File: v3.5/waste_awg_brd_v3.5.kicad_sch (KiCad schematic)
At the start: 24 parts, among them J1 Conn_01x06, U1 74HC595, U2 74HC595, U3 CA56-12CGKWA

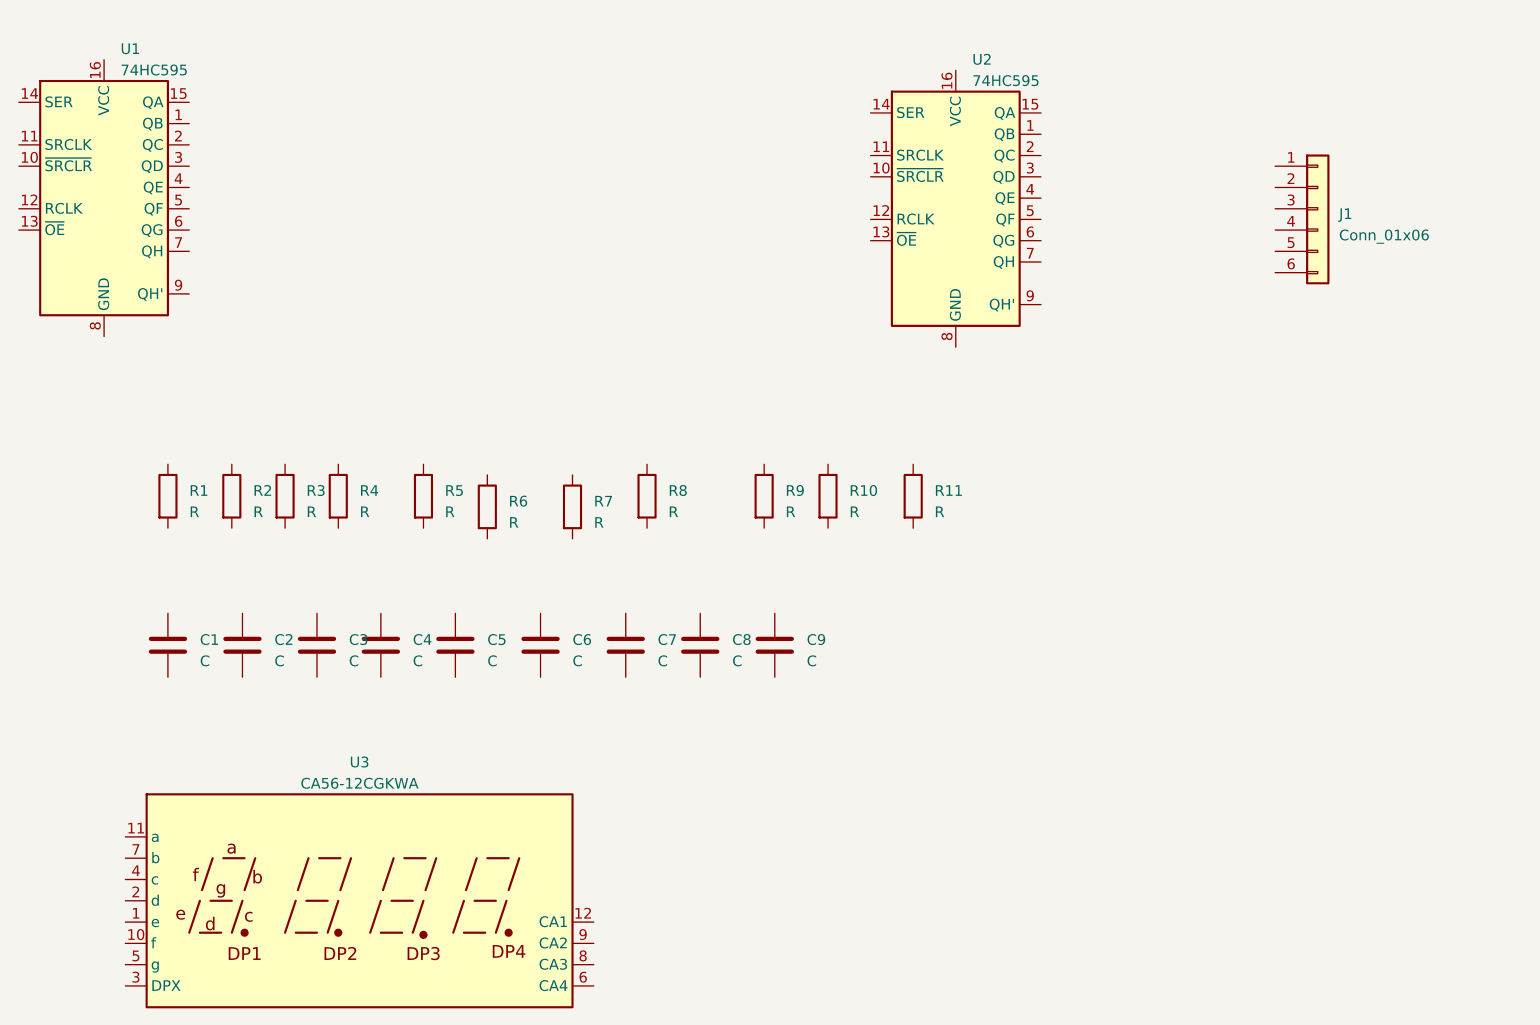
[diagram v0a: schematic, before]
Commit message: 初步建立各个元器件的关系
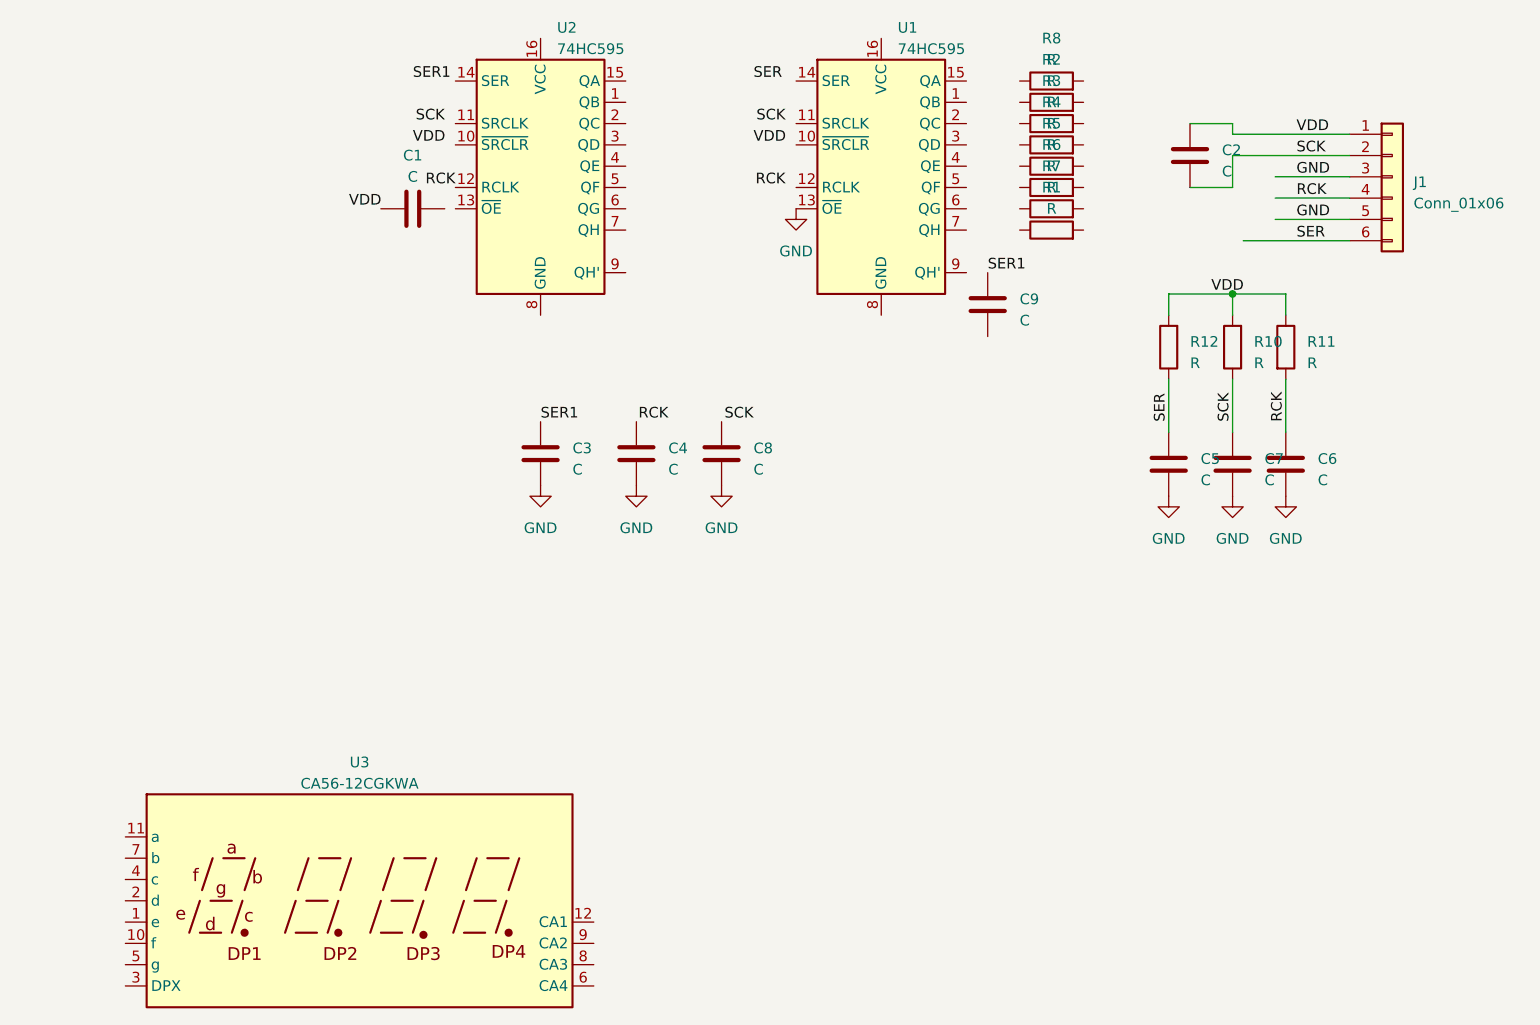
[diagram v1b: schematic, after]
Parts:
- removed R9: R, symbol Device:R
- added R12: R, symbol Device:R
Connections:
- net GND: now reaches U1.13 (~{OE})
- net GND: now also C3.2, C4.2, C5.2, C6.2, C7.2, C8.2, J1.3 (Pin_3), J1.5 (Pin_5)
- net RCK: now reaches C6.1
- net RCK: now also J1.4 (Pin_4), R11.2, U2.12 (RCLK)
- net SER: now reaches C5.1
- net SER: now also J1.6 (Pin_6), R12.1
- net SER1: now reaches C3.1
- net SER1: now also C9.1
- net VDD: now reaches J1.1 (Pin_1)
- net VDD: now also C2.1, R10.2, R11.1, R12.2
- net SCK: now reaches J1.2 (Pin_2)
- net SCK: now also C2.2, C7.1, R10.1
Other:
- moved on the sheet: C1, C2, C3, C4, C5, C6, C7, C8, C9, J1, R1, R10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
